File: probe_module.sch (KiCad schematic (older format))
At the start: 6 parts

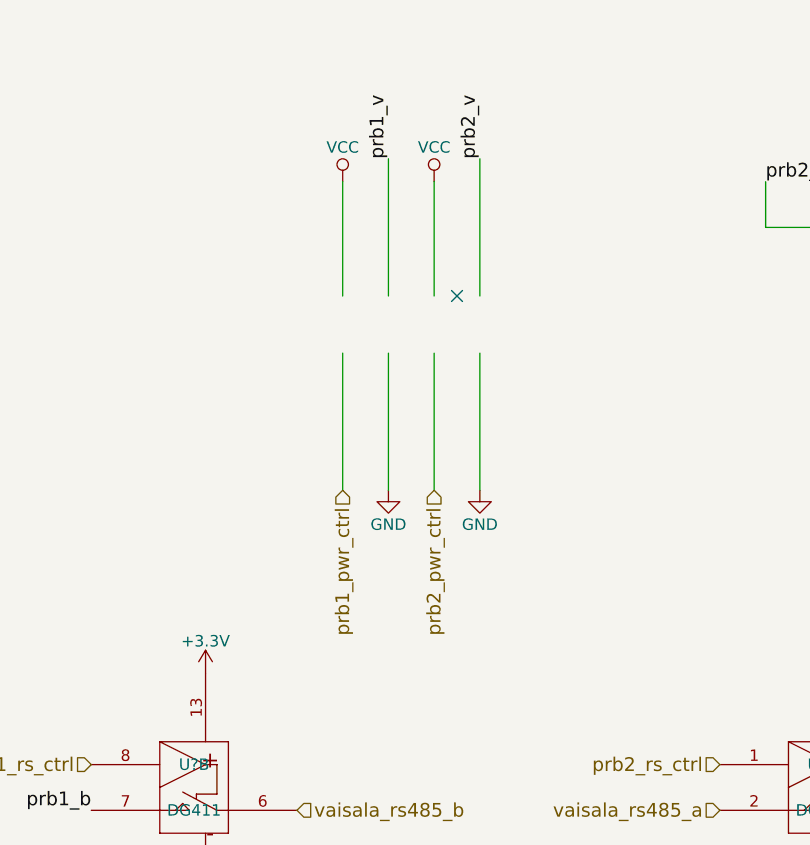
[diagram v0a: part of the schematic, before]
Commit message: change probe powerswitch to ssr
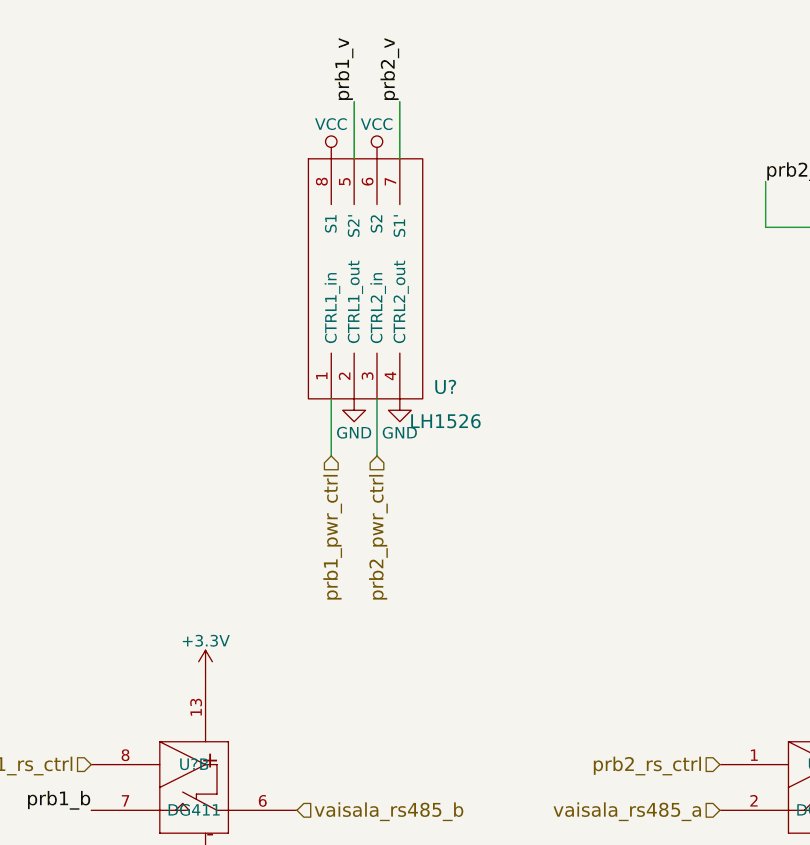
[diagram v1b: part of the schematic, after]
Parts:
- added U?: LH1526, symbol LH1526
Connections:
- wire segments 16 -> 12
- no-connect marks 3 -> 2
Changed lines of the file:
@@
 LIBS:ftdi
 LIBS:relays
+LIBS:components
+LIBS:pt-module-cache
 EELAYER 25 0
 EELAYER END
@@
 Text Label 3200 1900 3    60   ~ 0
 prb1_b
-Text HLabel 5300 3150 3    60   Input ~ 0
+Text HLabel 5250 3000 3    60   Input ~ 0
 prb1_pwr_ctrl
 Text HLabel 1850 4350 0    60   Input ~ 0
@@
 $EndComp
 NoConn ~ 3300 1900
-Text HLabel 5700 3150 3    60   Input ~ 0
+Text HLabel 5450 3000 3    60   Input ~ 0
 prb2_pwr_ctrl
 $Comp
@@
 L GND #PWR?
 U 1 1 5990A260
-P 5500 3150
-F 0 "#PWR?" H 5500 2900 50  0001 C CNN
-F 1 "GND" H 5500 3000 50  0000 C CNN
-F 2 "" H 5500 3150 50  0001 C CNN
-F 3 "" H 5500 3150 50  0001 C CNN
-	1    5500 3150
+P 5350 2750
+F 0 "#PWR?" H 5350 2500 50  0001 C CNN
+F 1 "GND" H 5350 2600 50  0000 C CNN
+F 2 "" H 5350 2750 50  0001 C CNN
+F 3 "" H 5350 2750 50  0001 C CNN
+	1    5350 2750
 	1    0    0    -1
 $EndComp
@@
 L GND #PWR?
 U 1 1 5990A28D
-P 5900 3150
-F 0 "#PWR?" H 5900 2900 50  0001 C CNN
-F 1 "GND" H 5900 3000 50  0000 C CNN
-F 2 "" H 5900 3150 50  0001 C CNN
-F 3 "" H 5900 3150 50  0001 C CNN
-	1    5900 3150
+P 5550 2750
+F 0 "#PWR?" H 5550 2500 50  0001 C CNN
+F 1 "GND" H 5550 2600 50  0000 C CNN
+F 2 "" H 5550 2750 50  0001 C CNN
+F 3 "" H 5550 2750 50  0001 C CNN
+	1    5550 2750
 	1    0    0    -1
 $EndComp
@@
 L VCC #PWR?
 U 1 1 5990AB6A
-P 5300 1800
-F 0 "#PWR?" H 5300 1650 50  0001 C CNN
-F 1 "VCC" H 5300 1950 50  0000 C CNN
-F 2 "" H 5300 1800 50  0001 C CNN
-F 3 "" H 5300 1800 50  0001 C CNN
-	1    5300 1800
+P 5250 1700
+F 0 "#PWR?" H 5250 1550 50  0001 C CNN
+F 1 "VCC" H 5250 1850 50  0000 C CNN
+F 2 "" H 5250 1700 50  0001 C CNN
+F 3 "" H 5250 1700 50  0001 C CNN
+	1    5250 1700
 	1    0    0    -1
 $EndComp
@@
 L VCC #PWR?
 U 1 1 5990AB9B
-P 5700 1800
-F 0 "#PWR?" H 5700 1650 50  0001 C CNN
-F 1 "VCC" H 5700 1950 50  0000 C CNN
-F 2 "" H 5700 1800 50  0001 C CNN
-F 3 "" H 5700 1800 50  0001 C CNN
-	1    5700 1800
+P 5450 1700
+F 0 "#PWR?" H 5450 1550 50  0001 C CNN
+F 1 "VCC" H 5450 1850 50  0000 C CNN
+F 2 "" H 5450 1700 50  0001 C CNN
+F 3 "" H 5450 1700 50  0001 C CNN
+	1    5450 1700
 	1    0    0    -1
 $EndComp
@@
 	3000 1900 3000 2250
 Wire Wire Line
-	5300 2550 5300 3150
-Wire Wire Line
-	5500 2550 5500 3150
-Wire Wire Line
-	5700 2550 5700 3150
-Wire Wire Line
-	5900 2550 5900 3150
-Wire Wire Line
 	7900 1800 7900 2150
-Wire Wire Line
-	5300 1800 5300 2300
-Wire Wire Line
-	5700 1800 5700 2300
 Text Label 2450 1850 0    60   ~ 0
 prb1_v
@@
 Wire Wire Line
 	7800 2000 7800 1800
-Text Label 5500 1700 1    60   ~ 0
+Text Label 5350 1450 1    60   ~ 0
 prb1_v
-Wire Wire Line
-	5500 1700 5500 2300
-Text Label 5900 1700 1    60   ~ 0
+Text Label 5550 1450 1    60   ~ 0
 prb2_v
-Wire Wire Line
-	5900 1700 5900 2300
-NoConn ~ 5800 2300
+$Comp
+L LH1526 U?
+U 1 1 5992F278
+P 5700 2800
+F 0 "U?" H 5750 2900 60  0000 C CNN
+F 1 "LH1526" H 5750 2750 60  0000 C CNN
+F 2 "" H 5750 2750 60  0001 C CNN
+F 3 "" H 5750 2750 60  0001 C CNN
+	1    5700 2800
+	1    0    0    -1
+$EndComp
+Wire Wire Line
+	5550 1450 5550 1700
+Wire Wire Line
+	5350 1450 5350 1700
+Wire Wire Line
+	5250 3000 5250 2750
+Wire Wire Line
+	5450 3000 5450 2750
 $EndSCHEMATC
